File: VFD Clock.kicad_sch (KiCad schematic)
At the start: 35 parts, among them J1 DS3231, J2 Mode Button, J3 Up Button, J4 Down Button, J5 Select Button, U1 74HC595, U10 74HC595, U11 UDN2981A, U12 IV-11 VFD Tube, U13 74HC595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

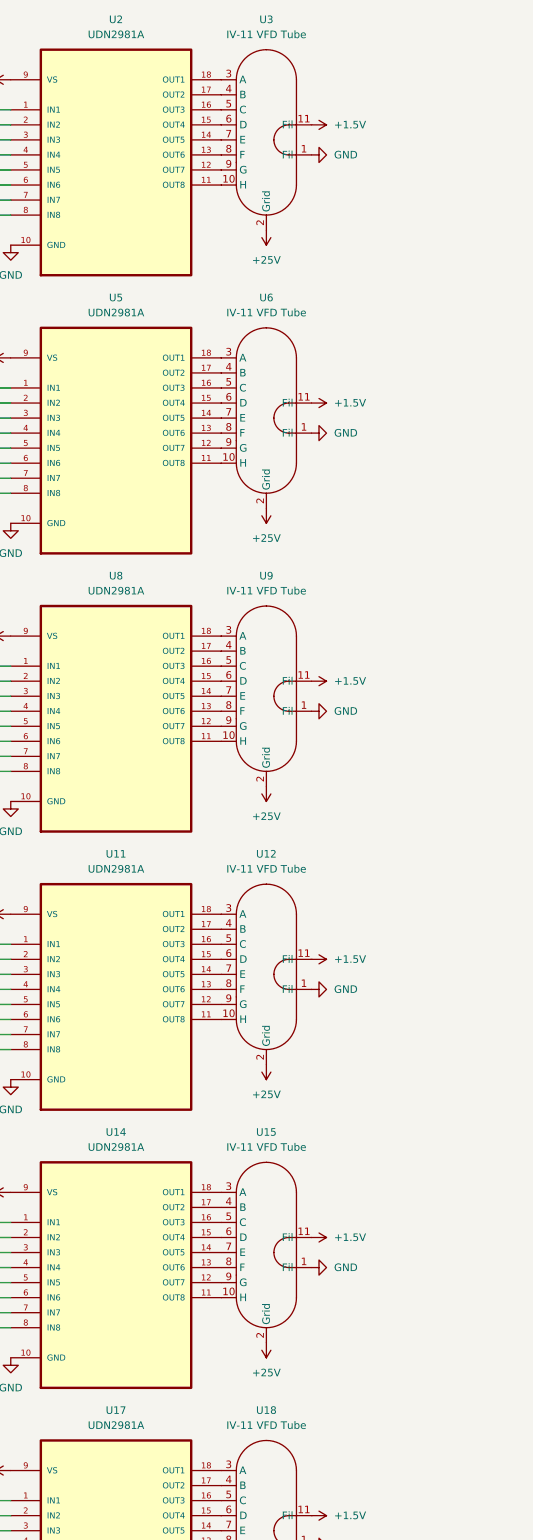
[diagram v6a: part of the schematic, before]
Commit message: pcb layout updates. Locked in the tube positions
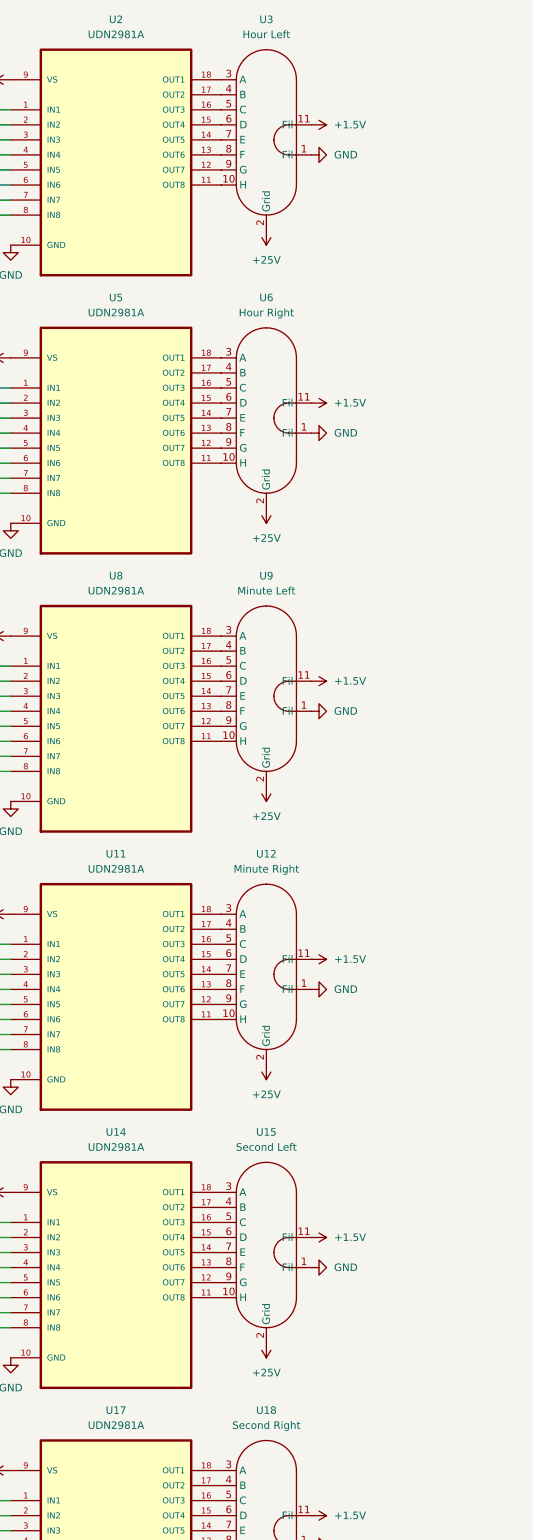
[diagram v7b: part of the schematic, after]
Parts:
- U12: value IV-11 VFD Tube -> Minute Right
- U15: value IV-11 VFD Tube -> Second Left
- U18: value IV-11 VFD Tube -> Second Right
- U3: value IV-11 VFD Tube -> Hour Left
- U6: value IV-11 VFD Tube -> Hour Right
- U9: value IV-11 VFD Tube -> Minute Left
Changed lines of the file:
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@@
 			)
 		)
-		(property "Value" "IV-11 VFD Tube"
+		(property "Value" "Hour Left"
 			(at 106.68 25.4 0)
 			(show_name no)
@@
 			)
 		)
-		(property "Value" "IV-11 VFD Tube"
+		(property "Value" "Minute Right"
 			(at 106.68 166.37 0)
 			(show_name no)
@@
 			)
 		)
-		(property "Value" "IV-11 VFD Tube"
+		(property "Value" "Hour Right"
 			(at 106.68 72.39 0)
 			(show_name no)
@@
 			)
 		)
-		(property "Value" "IV-11 VFD Tube"
+		(property "Value" "Second Left"
 			(at 106.68 213.36 0)
 			(show_name no)
@@
 			)
 		)
-		(property "Value" "IV-11 VFD Tube"
+		(property "Value" "Minute Left"
 			(at 106.68 119.38 0)
 			(show_name no)
@@
 			)
 		)
-		(property "Value" "IV-11 VFD Tube"
+		(property "Value" "Second Right"
 			(at 106.68 260.35 0)
 			(show_name no)

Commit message: PCB layout changes
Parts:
- removed D1: Power LED, symbol Device:LED
- removed R1: 220R, symbol Device:R_US
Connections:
- net Power LED: no longer names the net of A1.10 (D7)
- no-connect marks 1 -> 18
